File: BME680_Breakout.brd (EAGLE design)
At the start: 160 x 100 mm, 8 parts, among them U1 BME680

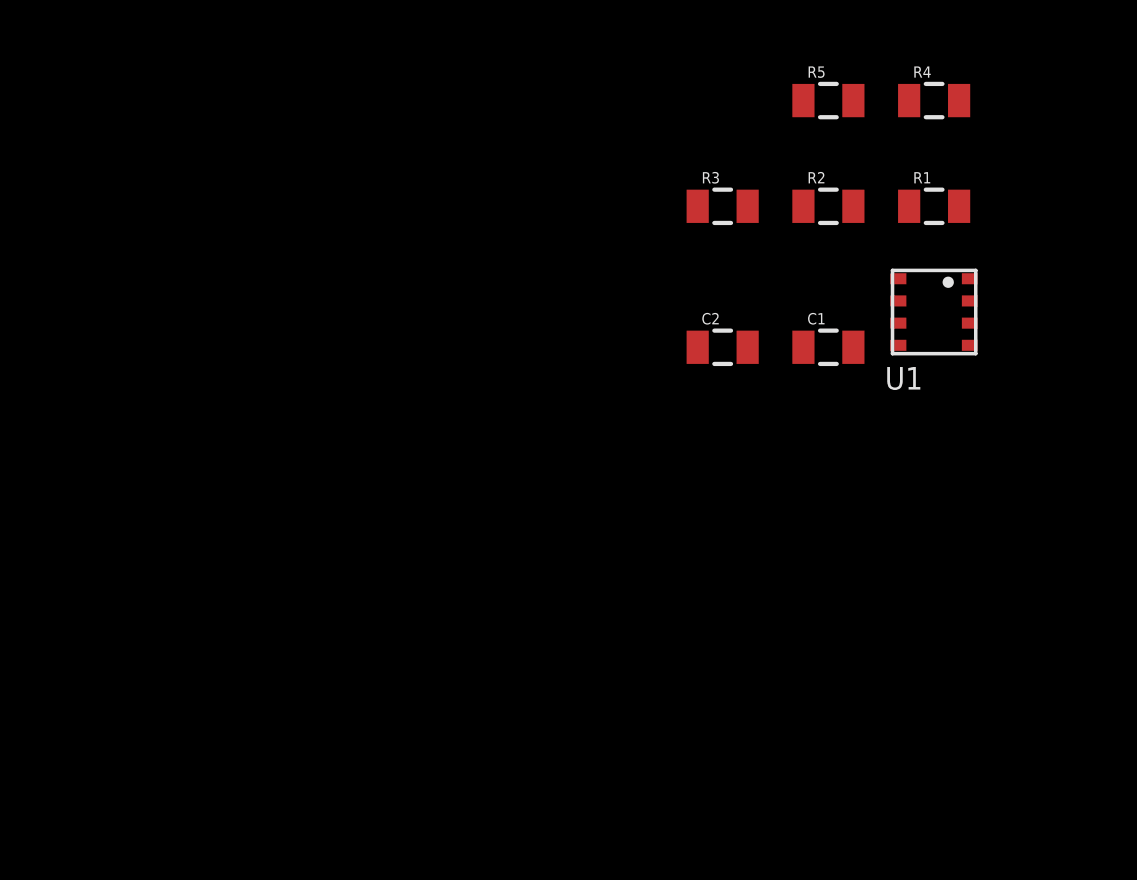
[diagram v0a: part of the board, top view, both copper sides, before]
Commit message: settled on i2c, renamed some signals, added level shifter logic
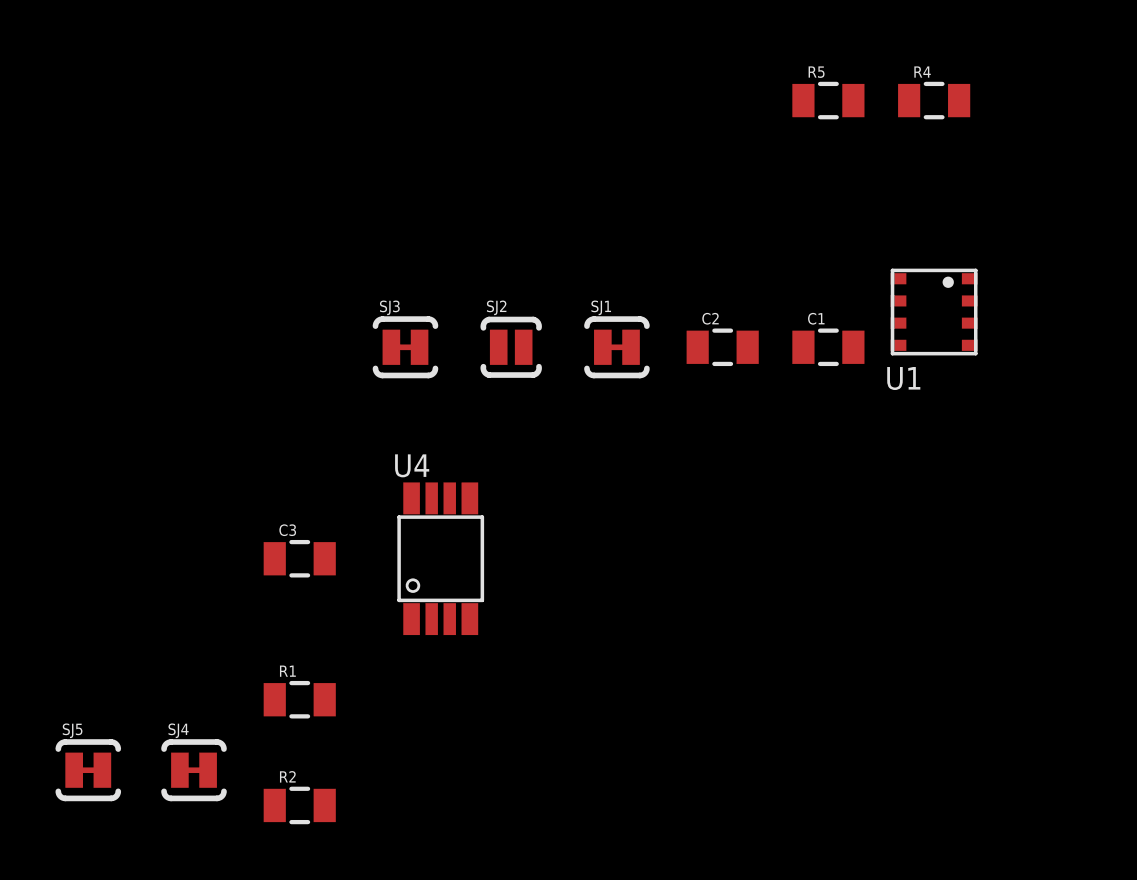
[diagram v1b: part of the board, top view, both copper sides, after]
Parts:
- removed R3: 0R, SparkFun-Passives:0805
- added C3: 0.1uF, SparkFun-Passives:0805
- added SJ1, SJ3, SJ4, SJ5: JUMPER-PAD-2-NC_BY_TRACE, SparkFun-Passives:PAD-JUMPER-2-NC_BY_TRACE_YES_SILK
- added SJ2: JUMPER-PAD-2-NOYES_SILK, SparkFun-Passives:PAD-JUMPER-2-NO_YES_SILK
- added U4: PCA9515ADP, PCA9515ADP:SOT505-1
- R1, R2: value 0R -> 4.7k
- moved R1 29.0 mm to (-38.1, -10.2)
- moved R2 28.8 mm to (-38.1, -14.0)
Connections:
- removed net SCK_SCL_3V3: R5.2, U1.4
- removed net SDI_SDA_3V3: R4.2, U1.3
- removed net SDO_ADDR_3V3: R1.1, R2.2, U1.5
- new net ADDR_SELECT_3V3: SJ1.2, SJ2.1, U1.5
- new net MASTER_SCL_3V3: SJ5.1
- new net MASTER_SCL_VIO: U4.2
- new net MASTER_SDA_3V3: SJ4.1
- new net MASTER_SDA_VIO: U4.3
- new net N$1: R1.2, SJ4.2
- new net N$2: R2.2, SJ5.2
- new net SLAVE_I2C_ENABLE: U4.5
- new net SLAVE_SCL_3V3: R5.2, U1.4, U4.7
- new net SLAVE_SDA_3V3: R4.2, U1.3, U4.6
- new net VCCIO: R1.1, R2.1
- net 3.3V: now also C3.1, SJ2.2, SJ3.2, U4.8; no longer R1.2, R3.2
- net CSB_3V3: now also SJ3.1; no longer R3.1
- net GND: now also C3.2, SJ1.1, U4.4; no longer R2.1
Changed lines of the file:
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@@
 <element name="C1" library="SparkFun-Passives" package="0805" value="0.1uF" x="-19.05" y="2.54"/>
 <element name="C2" library="SparkFun-Passives" package="0805" value="0.1uF" x="-22.86" y="2.54"/>
-<element name="R1" library="SparkFun-Passives" package="0805" value="0R" x="-15.24" y="7.62"/>
-<element name="R2" library="SparkFun-Passives" package="0805" value="0R" x="-19.05" y="7.62"/>
-<element name="R3" library="SparkFun-Passives" package="0805" value="0R" x="-22.86" y="7.62"/>
 <element name="R4" library="SparkFun-Passives" package="0805" value="4.7k" x="-15.24" y="11.43"/>
 <element name="R5" library="SparkFun-Passives" package="0805" value="4.7k" x="-19.05" y="11.43"/>
 <element name="U1" library="wicked-device" package="BME680" value="BME680" x="-15.24" y="3.81"/>
+<element name="SJ1" library="SparkFun-Passives" package="PAD-JUMPER-2-NC_BY_TRACE_YES_SILK" value="JUMPER-PAD-2-NC_BY_TRACE" x="-26.67" y="2.54"/>
+<element name="SJ2" library="SparkFun-Passives" package="PAD-JUMPER-2-NO_YES_SILK" value="JUMPER-PAD-2-NOYES_SILK" x="-30.48" y="2.54"/>
+<element name="SJ3" library="SparkFun-Passives" package="PAD-JUMPER-2-NC_BY_TRACE_YES_SILK" value="JUMPER-PAD-2-NC_BY_TRACE" x="-34.29" y="2.54"/>
+<element name="U4" library="PCA9515ADP" package="SOT505-1" value="PCA9515ADP" x="-33.02" y="-5.08"/>
+<element name="C3" library="SparkFun-Passives" package="0805" value="0.1uF" x="-38.1" y="-5.08"/>
+<element name="R1" library="SparkFun-Passives" package="0805" value="4.7k" x="-38.1" y="-10.16"/>
+<element name="R2" library="SparkFun-Passives" package="0805" value="4.7k" x="-38.1" y="-13.97"/>
+<element name="SJ4" library="SparkFun-Passives" package="PAD-JUMPER-2-NC_BY_TRACE_YES_SILK" value="JUMPER-PAD-2-NC_BY_TRACE" x="-41.91" y="-12.7"/>
+<element name="SJ5" library="SparkFun-Passives" package="PAD-JUMPER-2-NC_BY_TRACE_YES_SILK" value="JUMPER-PAD-2-NC_BY_TRACE" x="-45.72" y="-12.7"/>
 </elements>
 <signals>
@@
 <contactref element="C1" pad="1"/>
 <contactref element="C2" pad="1"/>
-<contactref element="R1" pad="2"/>
-<contactref element="R3" pad="2"/>
 <contactref element="R4" pad="1"/>
 <contactref element="R5" pad="1"/>
+<contactref element="SJ2" pad="2"/>
+<contactref element="SJ3" pad="2"/>
+<contactref element="U4" pad="8"/>
+<contactref element="C3" pad="1"/>
+<wire x1="-34.07" y1="-2.905" x2="-39" y2="-5.08" width="0" layer="19" extent="1-1"/>
+<wire x1="-33.782" y1="2.54" x2="-34.07" y2="-2.905" width="0" layer="19" extent="1-1"/>
+<wire x1="-30.03" y1="2.54" x2="-33.782" y2="2.54" width="0" layer="19" extent="1-1"/>
+<wire x1="-23.76" y1="2.54" x2="-30.03" y2="2.54" width="0" layer="19" extent="1-1"/>
 <wire x1="-19.95" y1="2.54" x2="-23.76" y2="2.54" width="0" layer="19" extent="1-1"/>
 <wire x1="-16.5275" y1="3.41" x2="-19.95" y2="2.54" width="0" layer="19" extent="1-1"/>
 <wire x1="-16.5275" y1="5.01" x2="-16.5275" y2="3.41" width="0" layer="19" extent="1-1"/>
-<wire x1="-14.34" y1="7.62" x2="-16.5275" y2="5.01" width="0" layer="19" extent="1-1"/>
-<wire x1="-16.14" y1="11.43" x2="-14.34" y2="7.62" width="0" layer="19" extent="1-1"/>
+<wire x1="-16.14" y1="11.43" x2="-16.5275" y2="5.01" width="0" layer="19" extent="1-1"/>
 <wire x1="-19.95" y1="11.43" x2="-16.14" y2="11.43" width="0" layer="19" extent="1-1"/>
-<wire x1="-21.96" y1="7.62" x2="-19.95" y2="11.43" width="0" layer="19" extent="1-1"/>
 </signal>
 <signal name="GND">
@@
 <contactref element="U1" pad="1"/>
 <contactref element="U1" pad="7"/>
-<contactref element="R2" pad="1"/>
+<contactref element="SJ1" pad="1"/>
+<contactref element="U4" pad="4"/>
+<contactref element="C3" pad="2"/>
+<wire x1="-31.97" y1="-7.255" x2="-37.2" y2="-5.08" width="0" layer="19" extent="1-1"/>
+<wire x1="-27.178" y1="2.54" x2="-31.97" y2="-7.255" width="0" layer="19" extent="1-1"/>
+<wire x1="-21.96" y1="2.54" x2="-27.178" y2="2.54" width="0" layer="19" extent="1-1"/>
 <wire x1="-18.15" y1="2.54" x2="-21.96" y2="2.54" width="0" layer="19" extent="1-1"/>
 <wire x1="-16.5275" y1="4.21" x2="-18.15" y2="2.54" width="0" layer="19" extent="1-1"/>
 <wire x1="-13.9525" y1="5.01" x2="-16.5275" y2="4.21" width="0" layer="19" extent="1-1"/>
-<wire x1="-19.95" y1="7.62" x2="-16.5275" y2="4.21" width="0" layer="19" extent="1-1"/>
 </signal>
 <signal name="CSB_3V3">
 <contactref element="U1" pad="2"/>
-<contactref element="R3" pad="1"/>
-<wire x1="-13.9525" y1="4.21" x2="-23.76" y2="7.62" width="0" layer="19" extent="1-1"/>
+<contactref element="SJ3" pad="1"/>
+<wire x1="-13.9525" y1="4.21" x2="-34.798" y2="2.54" width="0" layer="19" extent="1-1"/>
 </signal>
-<signal name="SDI_SDA_3V3">
+<signal name="ADDR_SELECT_3V3">
+<contactref element="U1" pad="5"/>
+<contactref element="SJ2" pad="1"/>
+<contactref element="SJ1" pad="2"/>
+<wire x1="-26.162" y1="2.54" x2="-30.93" y2="2.54" width="0" layer="19" extent="1-1"/>
+<wire x1="-16.5275" y1="2.61" x2="-26.162" y2="2.54" width="0" layer="19" extent="1-1"/>
+</signal>
+<signal name="SLAVE_SCL_3V3">
+<contactref element="U1" pad="4"/>
+<contactref element="R5" pad="2"/>
+<contactref element="U4" pad="7"/>
+<wire x1="-13.9525" y1="2.61" x2="-33.345" y2="-2.905" width="0" layer="19" extent="1-1"/>
+<wire x1="-18.15" y1="11.43" x2="-13.9525" y2="2.61" width="0" layer="19" extent="1-1"/>
+</signal>
+<signal name="MASTER_SCL_VIO">
+<contactref element="U4" pad="2"/>
+</signal>
+<signal name="MASTER_SDA_VIO">
+<contactref element="U4" pad="3"/>
+</signal>
+<signal name="SLAVE_I2C_ENABLE">
+<contactref element="U4" pad="5"/>
+</signal>
+<signal name="SLAVE_SDA_3V3">
+<contactref element="U4" pad="6"/>
 <contactref element="U1" pad="3"/>
 <contactref element="R4" pad="2"/>
+<wire x1="-13.9525" y1="3.41" x2="-32.695" y2="-2.905" width="0" layer="19" extent="1-1"/>
 <wire x1="-14.34" y1="11.43" x2="-13.9525" y2="3.41" width="0" layer="19" extent="1-1"/>
 </signal>
-<signal name="SCK_SCL_3V3">
-<contactref element="U1" pad="4"/>
-<contactref element="R5" pad="2"/>
-<wire x1="-18.15" y1="11.43" x2="-13.9525" y2="2.61" width="0" layer="19" extent="1-1"/>
+<signal name="VCCIO">
+<contactref element="R1" pad="1"/>
+<contactref element="R2" pad="1"/>
+<wire x1="-39" y1="-10.16" x2="-39" y2="-13.97" width="0" layer="19" extent="1-1"/>
 </signal>
-<signal name="SDO_ADDR_3V3">
-<contactref element="U1" pad="5"/>
+<signal name="N$1">
+<contactref element="R1" pad="2"/>
+<contactref element="SJ4" pad="2"/>
+<wire x1="-37.2" y1="-10.16" x2="-41.402" y2="-12.7" width="0" layer="19" extent="1-1"/>
+</signal>
+<signal name="N$2">
 <contactref element="R2" pad="2"/>
-<contactref element="R1" pad="1"/>
-<wire x1="-16.14" y1="7.62" x2="-16.5275" y2="2.61" width="0" layer="19" extent="1-1"/>
-<wire x1="-18.15" y1="7.62" x2="-16.14" y2="7.62" width="0" layer="19" extent="1-1"/>
+<contactref element="SJ5" pad="2"/>
+<wire x1="-37.2" y1="-13.97" x2="-45.212" y2="-12.7" width="0" layer="19" extent="1-1"/>
+</signal>
+<signal name="MASTER_SDA_3V3">
+<contactref element="SJ4" pad="1"/>
+</signal>
+<signal name="MASTER_SCL_3V3">
+<contactref element="SJ5" pad="1"/>
 </signal>
 </signals>
